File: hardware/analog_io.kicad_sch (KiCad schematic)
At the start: 33 parts, among them U1 TLV9162, U2 OPA1678

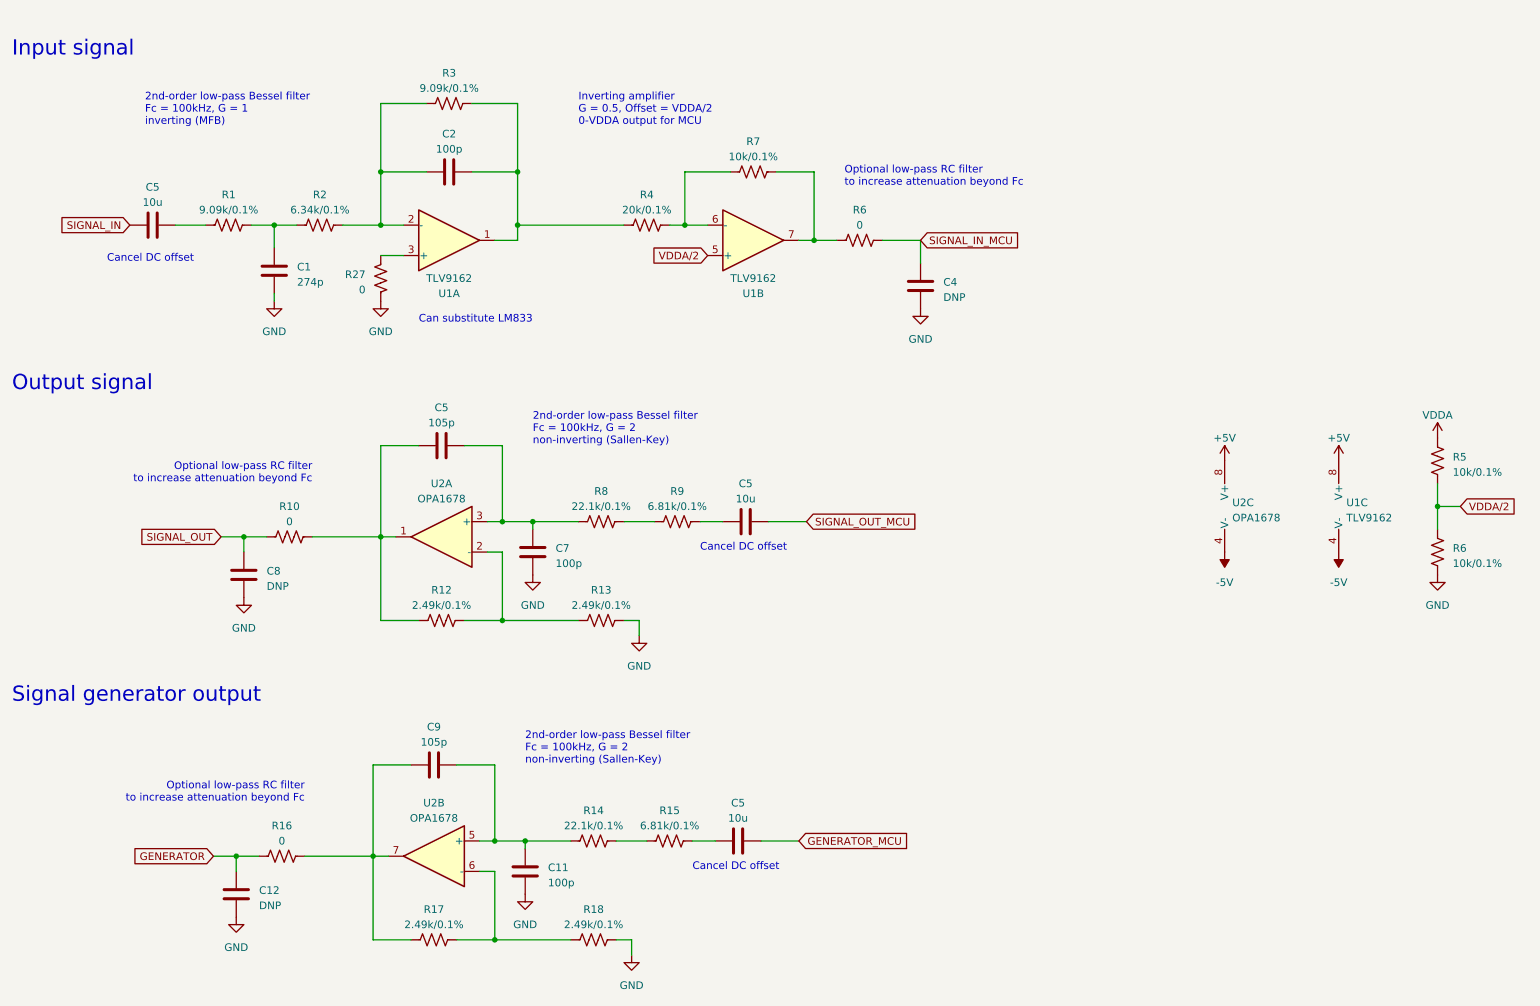
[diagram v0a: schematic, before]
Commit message: wip: schematic fixes based on testing
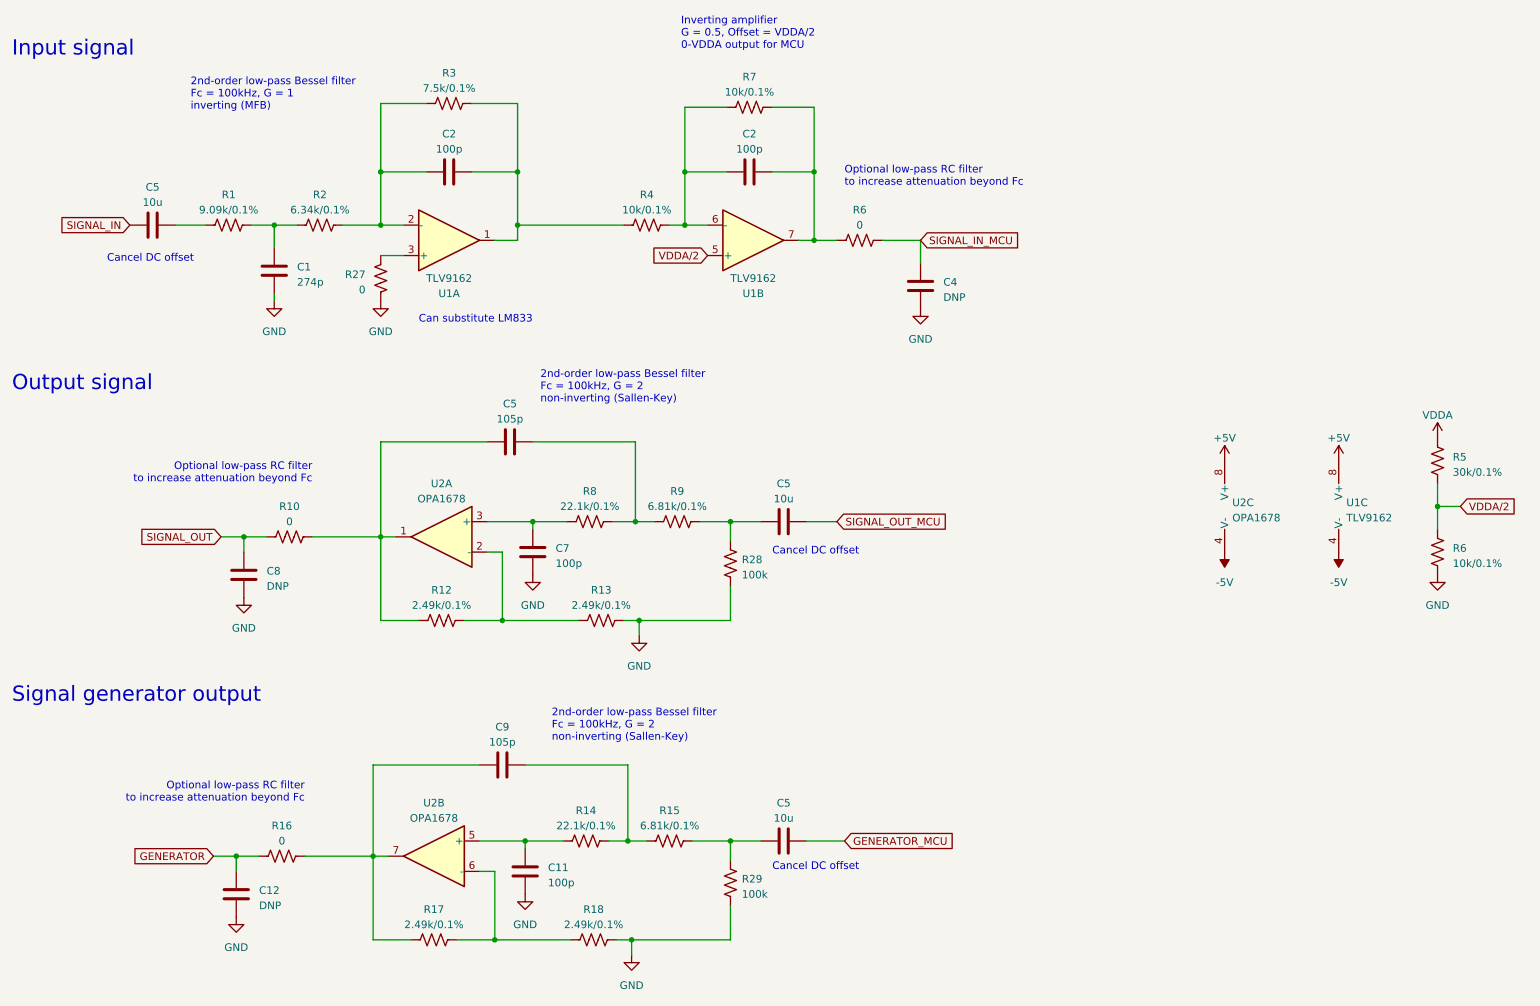
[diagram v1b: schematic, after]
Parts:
- added C2: 100p, Capacitor_SMD:C_0603_1608Metric, symbol Device:C
- added R28, R29: 100k, Resistor_SMD:R_0603_1608Metric, symbol Device:R_US
- R3: value 9.09k/0.1% -> 7.5k/0.1%; LCSC Part # C861611 -> (none); Part Number RT0603DRE079K09L -> (none)
- R4: value 20k/0.1% -> 10k/0.1%; LCSC Part # C5123584 -> (none); Part Number RT0603DRE0720KL -> (none)
- R5: value 10k/0.1% -> 30k/0.1%; LCSC Part # C319939 -> (none); Part Number RN73R1JTTD1002B25 -> (none)
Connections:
- net GND: now also R28.1, R29.1
- net at R4.2, R7.1, U1.6 (-): now also C2.1
- net at C11.1, R14.1, U2.5 (+): no longer C9.2
- net at R8.2, R9.1: now also C5.2
- net at C5.1, R9.2: now also R28.2
- net at C7.1, R8.1, U2.3 (+): no longer C5.2
- net at R14.2, R15.1: now also C9.2
- net at C5.1, R15.2: now also R29.2
- net at R6.1, R7.2, U1.7: now also C2.2
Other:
- moved on the sheet: C5, C9, R14, R7, R8

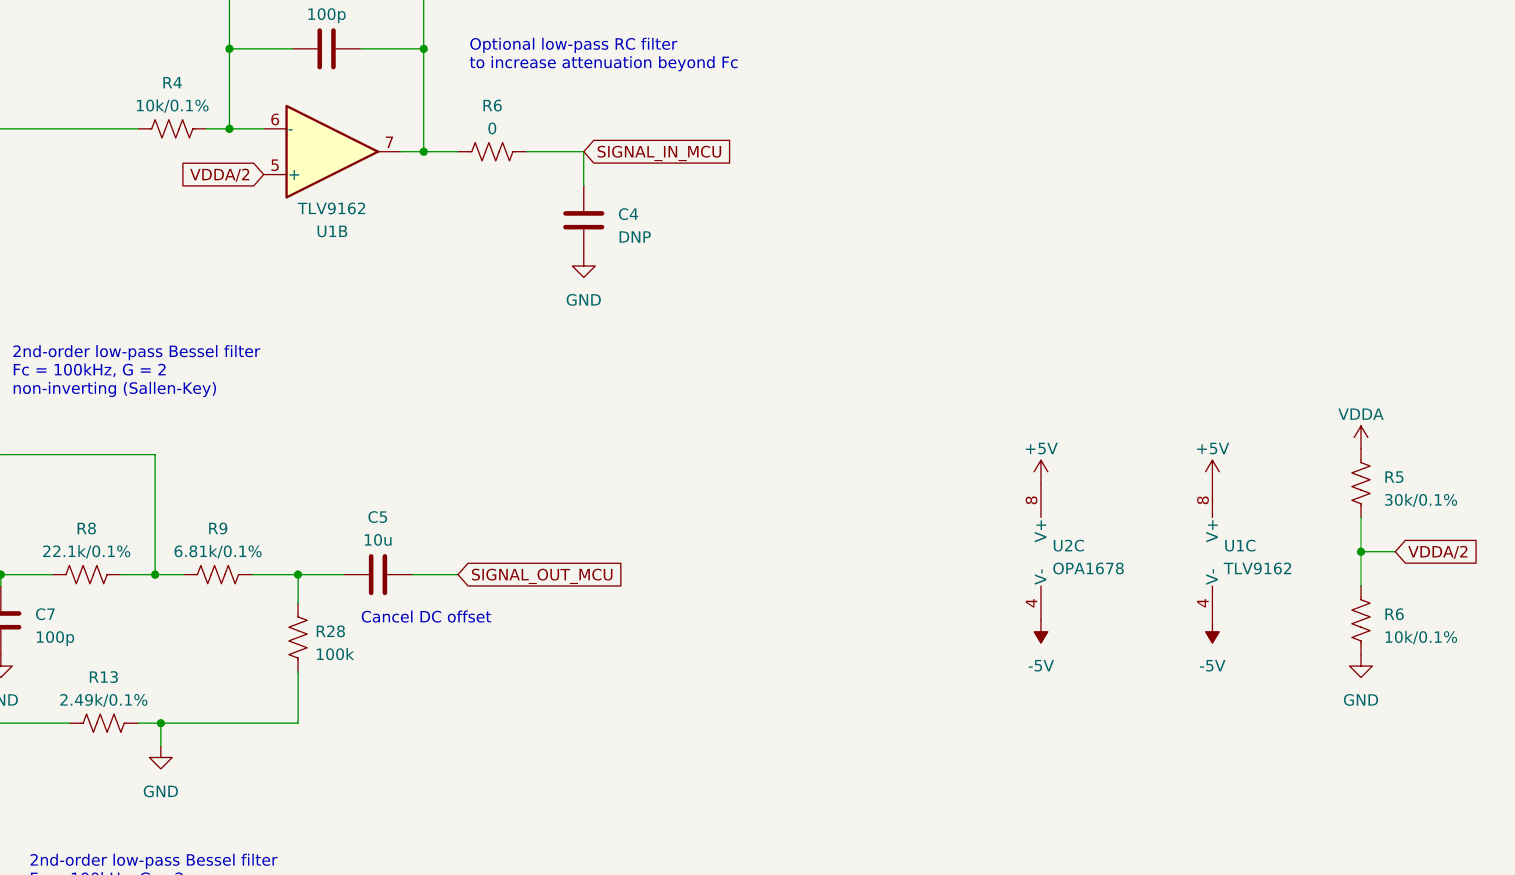
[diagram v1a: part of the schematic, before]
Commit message: vdda buffer; vdda for pots; other fixes
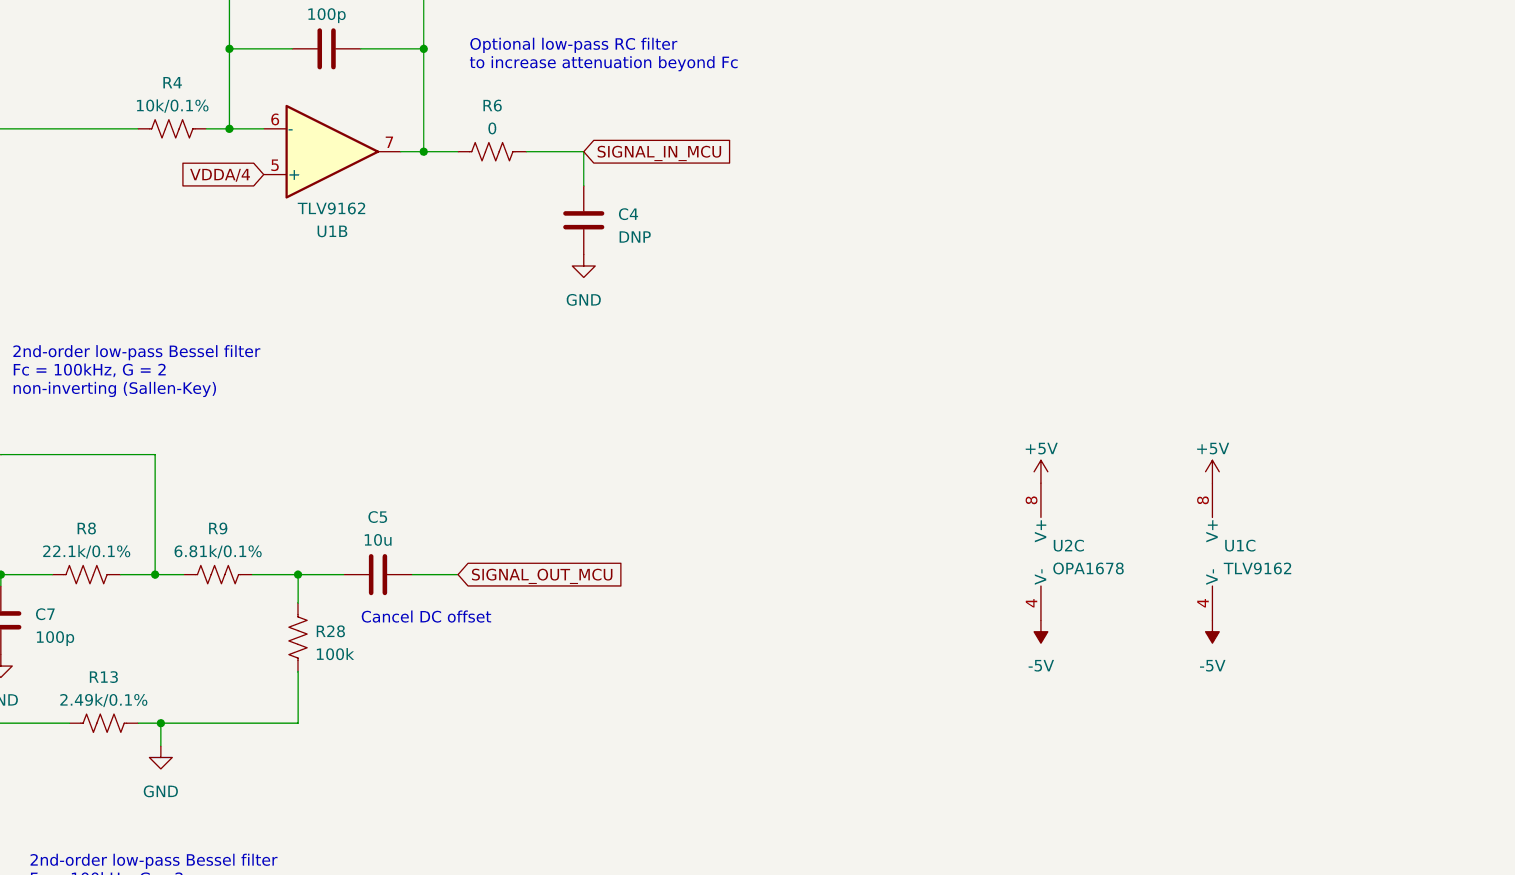
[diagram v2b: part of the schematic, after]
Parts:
- removed R5: 30k/0.1%, Resistor_SMD:R_0603_1608Metric, symbol Device:R_US
- removed R6: 10k/0.1%, Resistor_SMD:R_0603_1608Metric, symbol Device:R_US
- C1: LCSC Part # C107084 -> (none)
- C11, C2, C5, C7, C9: LCSC Part # C160903 -> (none)
- C5: LCSC Part # C15850 -> (none)
- R1: LCSC Part # C861611 -> (none)
- R10, R16, R27, R6: LCSC Part # C21189 -> (none)
- R12, R13, R17, R18: LCSC Part # C861299 -> (none)
- R14, R8: LCSC Part # C861759 -> (none)
- R15, R9: LCSC Part # C326739 -> (none)
- R2: LCSC Part # C861532 -> (none)
- R7: LCSC Part # C319939 -> (none)
- U1: LCSC Part # C54272 -> (none)
- U2: LCSC Part # C192421 -> (none)
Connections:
- net VDDA/2 renamed VDDA/4

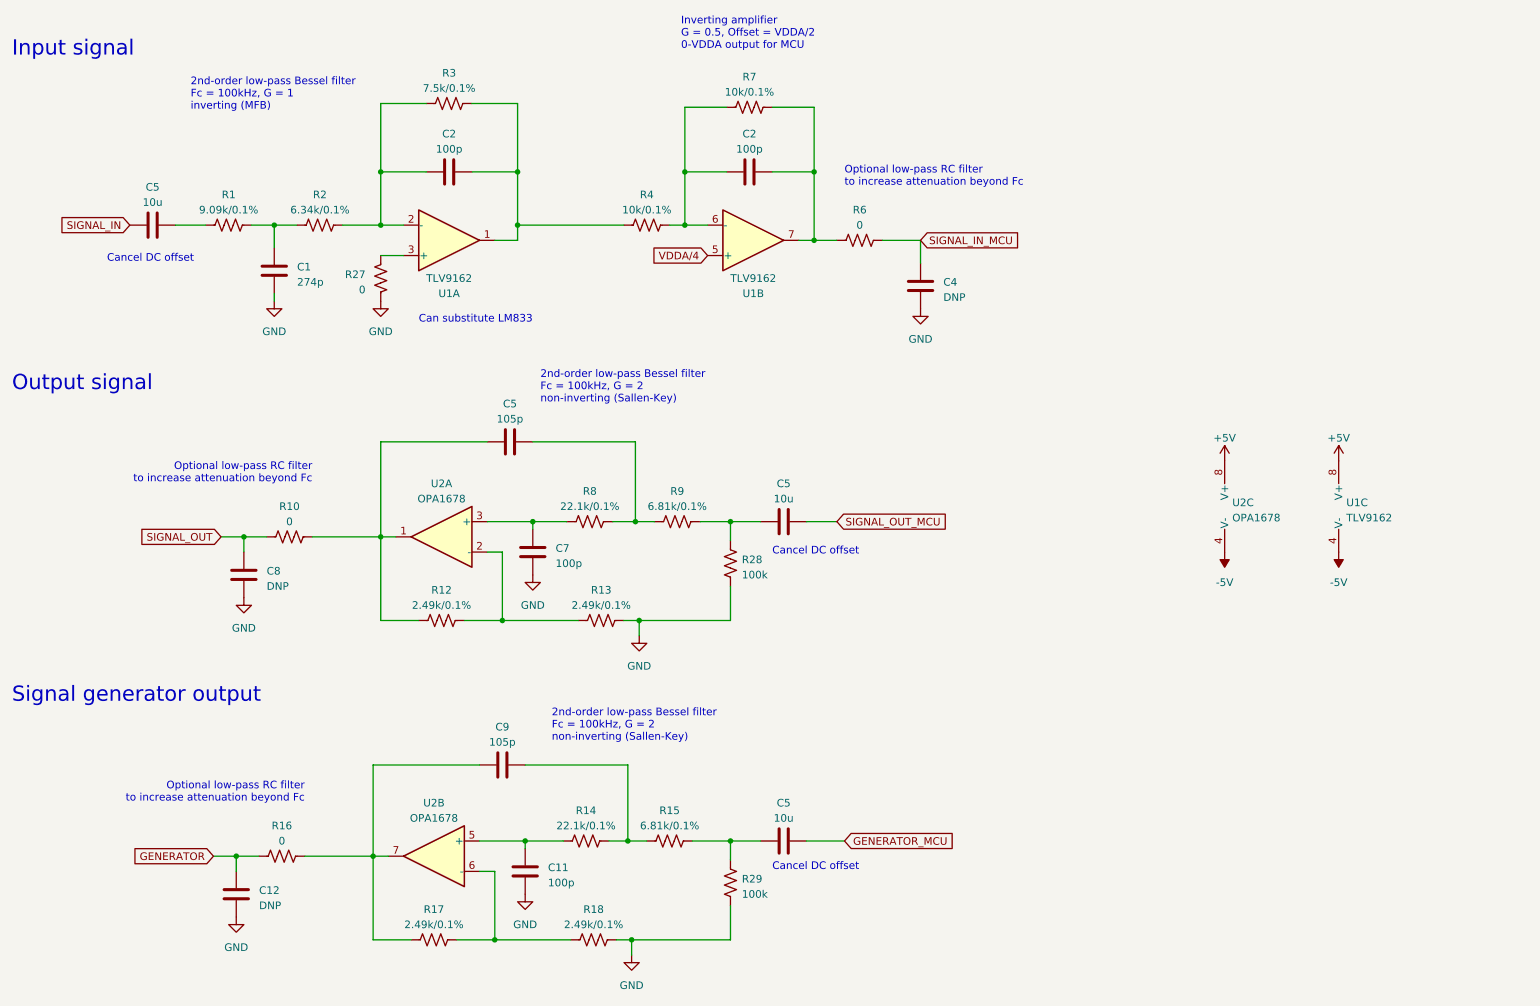
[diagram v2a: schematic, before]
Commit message: use nucleo 3.3v vdda; add 2nd low-pass stage to input
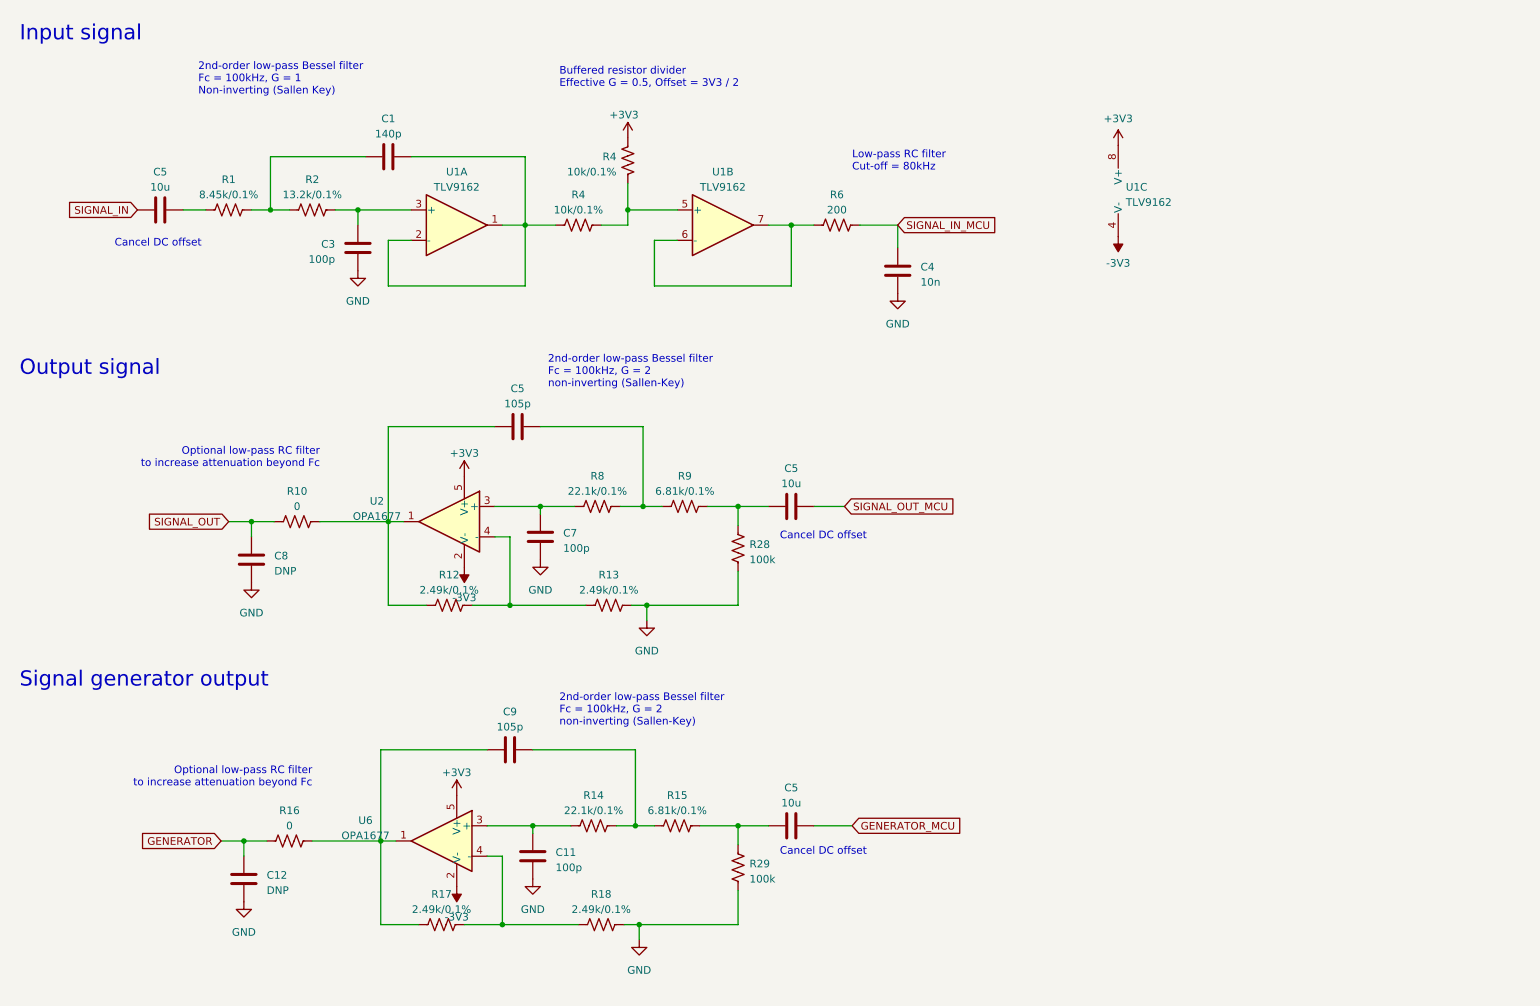
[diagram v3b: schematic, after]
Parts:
- removed C2 (x2): 100p, Capacitor_SMD:C_0603_1608Metric, symbol Device:C
- removed R27: 0, Resistor_SMD:R_0603_1608Metric, symbol Device:R_US
- removed R3: 7.5k/0.1%, Resistor_SMD:R_0603_1608Metric, symbol Device:R_US
- removed R7: 10k/0.1%, Resistor_SMD:R_0603_1608Metric, symbol Device:R_US
- removed U2: OPA1678, Package_SO:SOIC-8_3.9x4.9mm_P1.27mm, symbol Amplifier_Operational:TLV9062xD
- added C3: 100p, Capacitor_SMD:C_0603_1608Metric, symbol Device:C
- added R4: 10k/0.1%, Resistor_SMD:R_0603_1608Metric, symbol Device:R_US
- added U2, U6: OPA1677, Package_TO_SOT_SMD:SOT-23-5, symbol Amplifier_Operational:OPA196xDBV
- C1: value 274p -> 140p; Part Number CC0603KRX7R9BB271 -> (none)
- C4: value DNP -> 10n; DNP T -> (none)
- R1: value 9.09k/0.1% -> 8.45k/0.1%; Part Number RT0603DRE079K09L -> (none)
- R2: value 6.34k/0.1% -> 13.2k/0.1%; Part Number RT0603DRE076K34L -> (none)
- R6: value 0 -> 200; Part Number RMCF0603ZT0R00 -> (none)
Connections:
- net VDDA/4 is gone; now on an unnamed net: U1.5 (+)
- net GND: now also C3.2; no longer C1.2
- net at R4.1, U1.1: now also C1.2, U1.2 (-)
- net at R4.2: now also R4.1; no longer U1.6 (-)
- net at C9.1, R16.2, R17.1: now also U6.1
- net at R17.2, R18.1: now also U6.4 (-)
- net at C11.1, R14.1: now also U6.3 (+)
- net at R6.1, U1.7: now also U1.6 (-)
- net at C5.1, R10.2, R12.1: now also U2.1
- net at R12.2, R13.1: now also U2.4 (-)
- net at U1.3 (+): now also R2.2, C3.1
- net at C7.1, R8.1: now also U2.3 (+)
- net +5V renamed +3V3
- net +3V3: now also R4.2, U2.5 (V+), U6.5 (V+)
- net -5V renamed -3V3
- net -3V3: now also U2.2 (V-), U6.2 (V-)
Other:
- note added: "2nd-order low-pass Bessel filter Fc = 100kHz, G = 1 Non-inverting (Sallen Key)"
- note added: "Buffered resistor divider Effective G = 0.5, Offset = 3V3 / 2"
- note added: "Low-pass RC filter Cut-off = 80kHz"
- note removed: "2nd-order low-pass Bessel filter Fc = 100kHz, G = 1 inverting (MFB)"
- note removed: "Can substitute LM833"
- note removed: "Inverting amplifier G = 0.5, Offset = VDDA/2 0-VDDA output for MCU"
- moved on the sheet: C11, C12, C4, C5, C7, C8, C9, R1, R10, R12, R13, R14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
